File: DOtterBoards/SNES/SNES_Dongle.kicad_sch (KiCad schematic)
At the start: 11 parts, among them J1 SNES3, J2 SNES4, J3 IDC_2x03

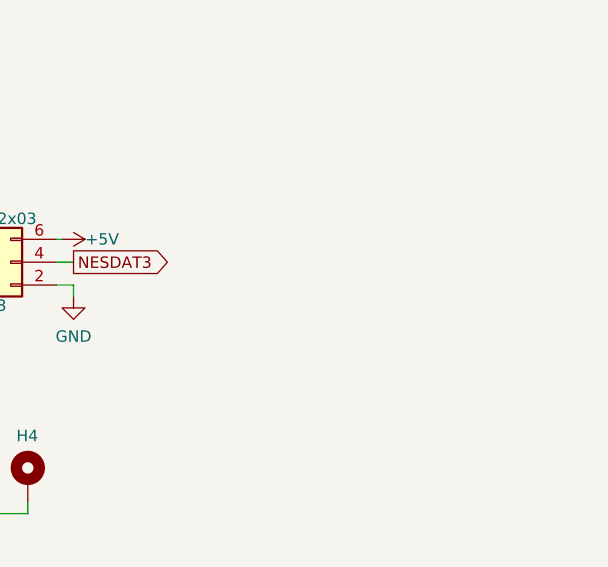
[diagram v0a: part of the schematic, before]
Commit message: Rename dongle boards to D'Otterboards
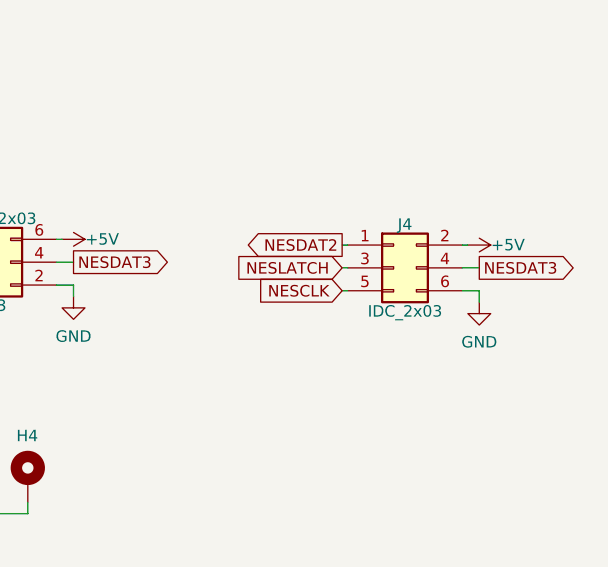
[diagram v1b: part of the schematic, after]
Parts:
- added J4: IDC_2x03, Connector_IDC:IDC-Header_2x03_P2.54mm_Vertical, symbol Connector_Generic:Conn_02x03_Odd_Even
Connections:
- net +5V: now also J4.2 (Pin_2)
- net GND: now also J4.6 (Pin_6)
- net NESCLK: now also J4.5 (Pin_5)
- net NESDAT2: now also J4.1 (Pin_1)
- net NESDAT3: now also J4.4 (Pin_4)
- net NESLATCH: now also J4.3 (Pin_3)
